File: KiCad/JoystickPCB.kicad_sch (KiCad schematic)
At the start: 6 parts, among them J1 B6B-PH-SM4-TB, U1 Pico, U2 ADS1115IDGSR

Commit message: Schematic should be finished
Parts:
- removed J1: B6B-PH-SM4-TB, Library:JST_B6B-PH-SM4-TB, symbol B6B-PH-SM4-TB:B6B-PH-SM4-TB
- removed U1: Pico, Library:MODULE_SC0915, symbol SC0915:SC0915
- added C2, C3: 10uF, Capacitor_SMD:C_0603_1608Metric, symbol Device:C
- added C4, C5: 0.1uF, Capacitor_SMD:C_0603_1608Metric, symbol Device:C
- added J1, J2: B4B-PH-SM4-TBT, Library:JST_B4B-PH-SM4-TBT, symbol B4B-PH-SM4-TBT:B4B-PH-SM4-TBT
- added Q1: ~, Package_TO_SOT_SMD:SOT-363_SC-70-6, symbol BSS138BKS:BSS138BKS
- added R3, R4, R5, R6: 10k, Resistor_SMD:R_0603_1608Metric, symbol Device:R
- added U3: ICM-20948, Sensor_Motion:InvenSense_QFN-24_3x3mm_P0.4mm, symbol Sensor_Motion:ICM-20948
- added U4: MIC5225-1.8YM5-TR, SOT-23-5_M5_MCH, symbol MIC5225-1.8V:MIC5225-1.8YM5-TR
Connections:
- net A0: now also J2.3
- net A1: now also J2.4
- net GND: now also C2.2, C3.2, C4.2, C5.2, J1.2, J2.2, U3.11 (FSYNC), U3.18 (GND), U3.20 (GND), U4.2 (GND)
- net SCL: now also J1.4, Q1.6 (D1), R6.1
- net SDA: now also J1.3, Q1.3 (D2), R3.1
- net A3.3V renamed 3.3V
- net 3.3V: now also J1.1, J2.1
- new net: C5.1, U3.10 (REGOUT)
- new net: C2.1, U4.1 (IN), U4.3 (EN)
- new net 1.8V: C3.1, C4.1, Q1.2 (G1), Q1.5 (G2), R3.2, R4.1, R5.1, R6.2, U3.13 (VDD), U3.22 (~{CS}), U3.8 (VDDIO), U3.9 (SDO/AD0), U4.5 (OUT)
- new net SCL_1.8V: Q1.1 (S1), R4.2, U3.23 (SCL/SCLK)
- new net SDA_1.8V: Q1.4 (S2), R5.2, U3.24 (SDA/SDI)
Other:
- note added: "1.1"
- note added: "11/6/2024"
- note added: "ADC"
- note added: "By Robbie Leslie"
- note added: "I2C Pullup"
- note added: "IMU"
- note added: "Power Supply"
- note added: "To Joystick"
- note added: "To Pico"
- note removed: "10/21/2024"
- moved on the sheet: C1, R1, R2, U2

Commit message: Started work on PCB design
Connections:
- net AGND is gone; now on net GND: C1.2, U2.3 (GND)
- net 3.3V: now also C2.1, U4.1 (IN), U4.3 (EN)
- net A1: now also J2.2; no longer J2.4
- net GND: now also J2.4; no longer J2.2

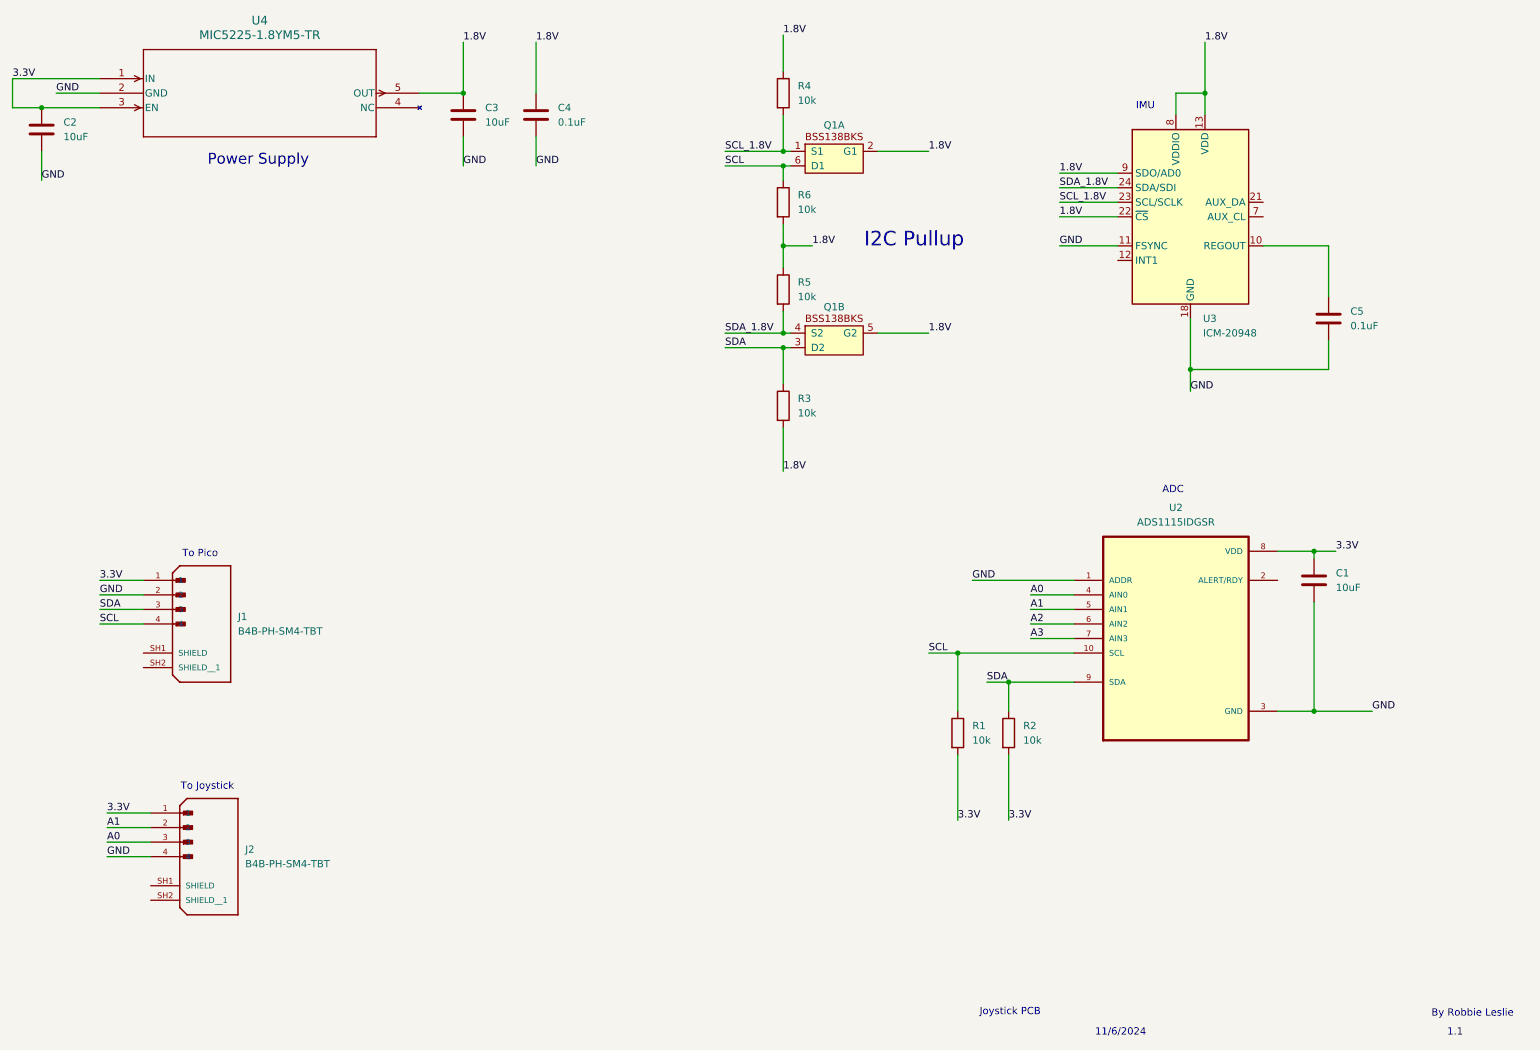
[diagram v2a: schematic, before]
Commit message: Added notes about future revisions
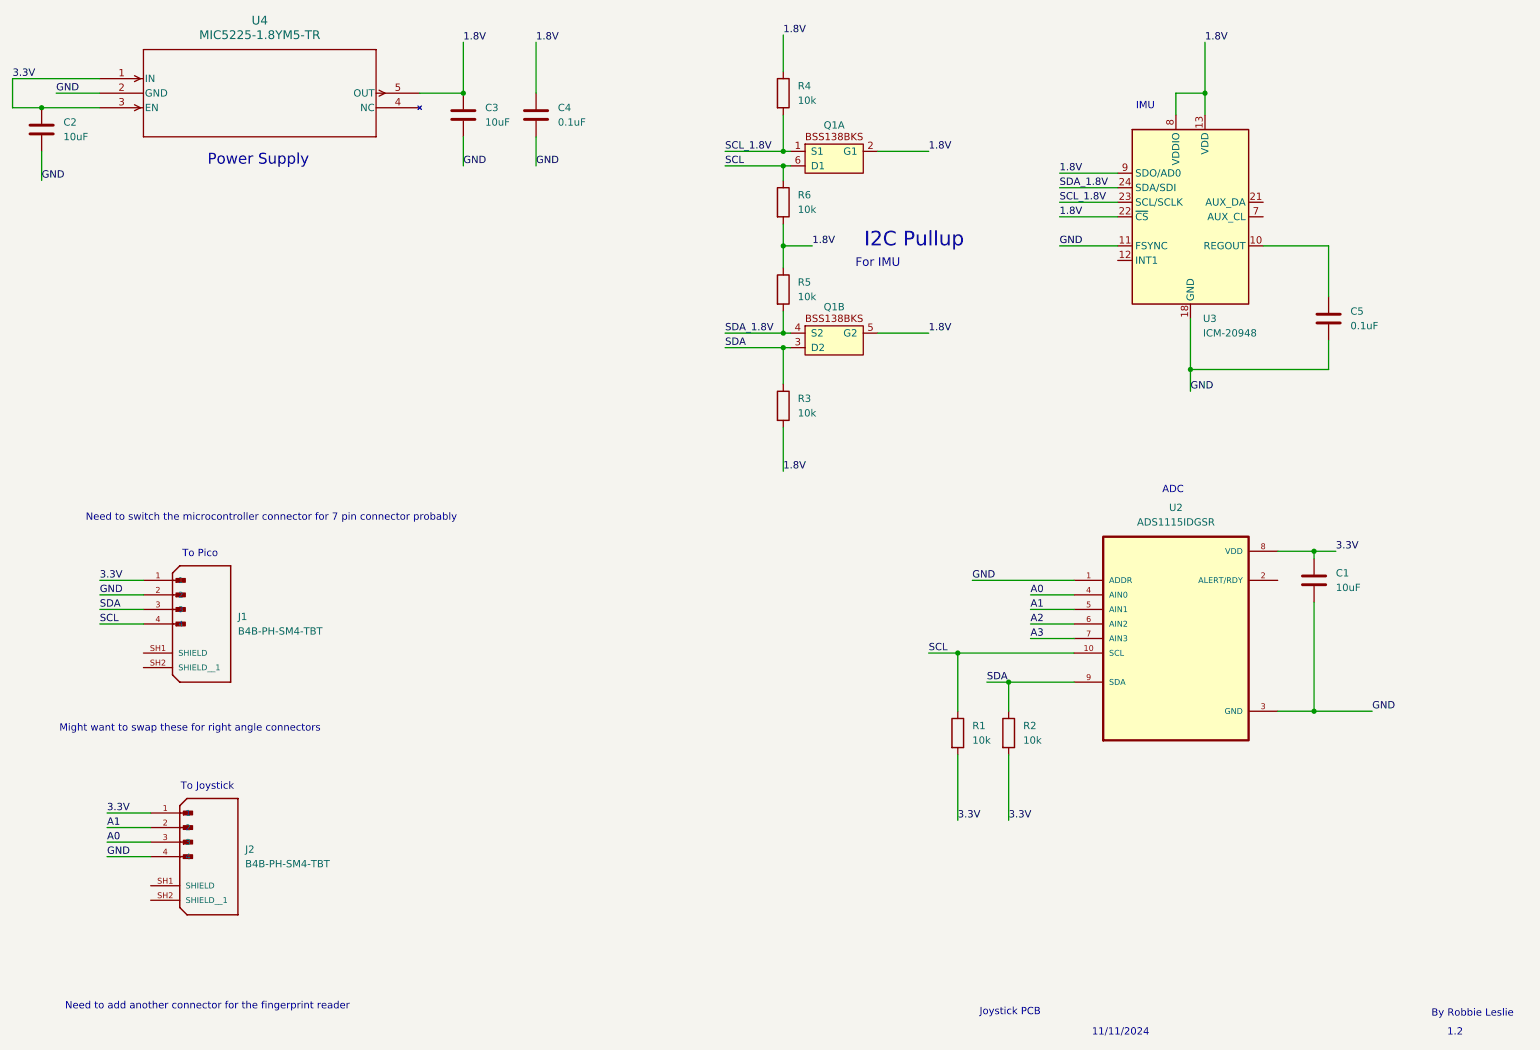
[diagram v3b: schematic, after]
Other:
- note added: "1.2"
- note added: "11/11/2024"
- note added: "For IMU"
- note added: "Might want to swap these for right angle connectors"
- note added: "Need to add another connector for the fingerprint reader"
- note added: "Need to switch the microcontroller connector for 7 pin connector probably"
- note removed: "1.1"
- note removed: "11/6/2024"
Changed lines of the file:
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@@
 		)
 	)
-	(text "1.1"
+	(text "For IMU"
+		(exclude_from_sim no)
+		(at 170.18 58.928 0)
+		(effects
+			(font
+				(size 1.5 1.5)
+			)
+		)
+	)
+	(text "1.2"
 		(exclude_from_sim no)
 		(at 271.018 193.294 0)
@@
 		)
 	)
-	(text "11/6/2024\n"
+	(text "11/11/2024\n"
 		(exclude_from_sim no)
 		(at 212.598 193.294 0)
@@
 		)
 	)
+	(text "Need to add another connector for the fingerprint reader"
+		(exclude_from_sim no)
+		(at 53.086 188.722 0)
+		(effects
+			(font
+				(size 1.27 1.27)
+			)
+		)
+	)
 	(text "Joystick PCB"
 		(exclude_from_sim no)
 		(at 193.294 189.738 0)
+		(effects
+			(font
+				(size 1.27 1.27)
+			)
+		)
+	)
+	(text "Need to switch the microcontroller connector for 7 pin connector probably "
+		(exclude_from_sim no)
+		(at 64.262 103.378 0)
 		(effects
 			(font
@@
 		(effects
 			(font
+				(size 1.27 1.27)
+			)
+		)
+	)
+	(text "Might want to swap these for right angle connectors"
+		(exclude_from_sim no)
+		(at 50.038 140.208 0)
+		(effects
+			(font
